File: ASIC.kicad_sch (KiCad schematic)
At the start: 74 parts, among them U12 TLV75512PDQNR, U14 TLV75512PDQNR, U15 TLV75512PDQNR, U3 TLV75512PDQNR, U8 SN74AVC4T774, Y2 50MHz

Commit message: power plane cleanup. added field vias. generated BOM
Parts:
- Y2: LCSC C5137267 -> (none)
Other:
- moved on the sheet: C19, C25, C26, C27, C28, C57, C58, C59, C68, C7, C72, R26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

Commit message: update TPS546D24 to `S` variant. Add render and readme.
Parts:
- TP18, TP2, TP3, TP4, TP58, TP59, TP60: now left out of the parts list
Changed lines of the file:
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@@
 		(unit 1)
 		(exclude_from_sim yes)
-		(in_bom yes)
+		(in_bom no)
 		(on_board yes)
 		(dnp no)
@@
 		(unit 1)
 		(exclude_from_sim yes)
-		(in_bom yes)
+		(in_bom no)
 		(on_board yes)
 		(dnp no)
@@
 		(unit 1)
 		(exclude_from_sim yes)
-		(in_bom yes)
+		(in_bom no)
 		(on_board yes)
 		(dnp no)
@@
 		(unit 1)
 		(exclude_from_sim yes)
-		(in_bom yes)
+		(in_bom no)
 		(on_board yes)
 		(dnp no)
@@
 		(unit 1)
 		(exclude_from_sim yes)
-		(in_bom yes)
+		(in_bom no)
 		(on_board yes)
 		(dnp no)
@@
 		(unit 1)
 		(exclude_from_sim yes)
-		(in_bom yes)
+		(in_bom no)
 		(on_board yes)
 		(dnp no)
@@
 		(unit 1)
 		(exclude_from_sim yes)
-		(in_bom yes)
+		(in_bom no)
 		(on_board yes)
 		(dnp no)

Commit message: unify 1k resistor part numbers
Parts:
- U8: value SN74AVC4T774 -> SN74AXC4T774
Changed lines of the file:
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@@
 			)
 		)
-		(property "Value" "SN74AVC4T774"
+		(property "Value" "SN74AXC4T774"
 			(at 502.92 306.07 0)
 			(effects

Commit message: update 50MHz osc part number.
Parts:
- Y2: DK (none) -> ECS-3225MV-500-CN-TR; PARTNO SX3M50.000E20F30THN -> XC2889CT-ND
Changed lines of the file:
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@@
 			)
 		)
-		(property "DK" ""
+		(property "DK" "ECS-3225MV-500-CN-TR"
 			(at 62.23 320.04 0)
 			(effects
@@
 			)
 		)
-		(property "PARTNO" "SX3M50.000E20F30THN"
+		(property "PARTNO" "XC2889CT-ND"
 			(at 62.23 320.04 0)
 			(effects

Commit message: change Y2 OSC part number back.
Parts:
- Y2: DK ECS-3225MV-500-CN-TR -> 5852-SX3M50.000E20F30THNTR-ND; LCSC (none) -> C5137267; PARTNO XC2889CT-ND -> SX3M50.000E20F30THN
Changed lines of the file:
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@@
 			)
 		)
-		(property "DK" "ECS-3225MV-500-CN-TR"
+		(property "DK" "5852-SX3M50.000E20F30THNTR-ND"
 			(at 62.23 320.04 0)
 			(effects
@@
 			)
 		)
-		(property "PARTNO" "XC2889CT-ND"
+		(property "PARTNO" "SX3M50.000E20F30THN"
 			(at 62.23 320.04 0)
 			(effects
@@
 			)
 		)
-		(property "LCSC" ""
+		(property "LCSC" "C5137267"
 			(at 62.23 320.04 0)
 			(effects

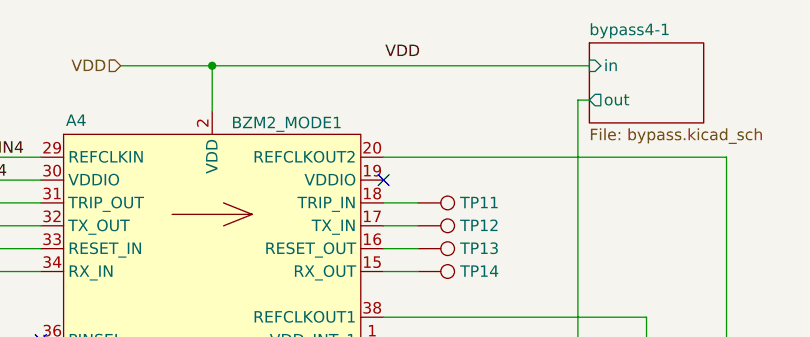
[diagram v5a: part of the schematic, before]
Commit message: clean up some of the schematic errors for #4
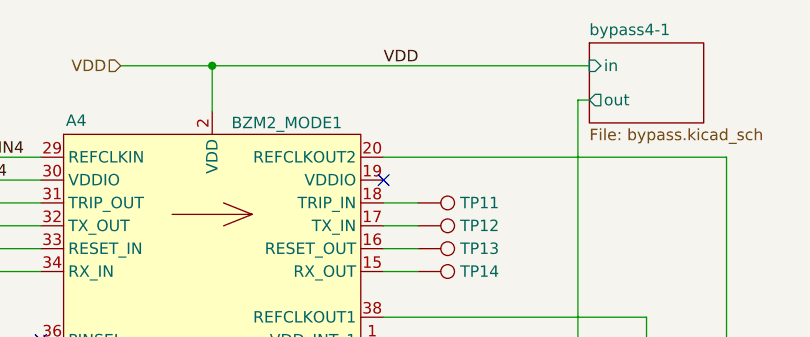
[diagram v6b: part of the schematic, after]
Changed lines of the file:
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@@
 	)
 	(label "VDD"
-		(at 306.2448 61.6474 0)
+		(at 306.07 62.23 0)
 		(effects
 			(font

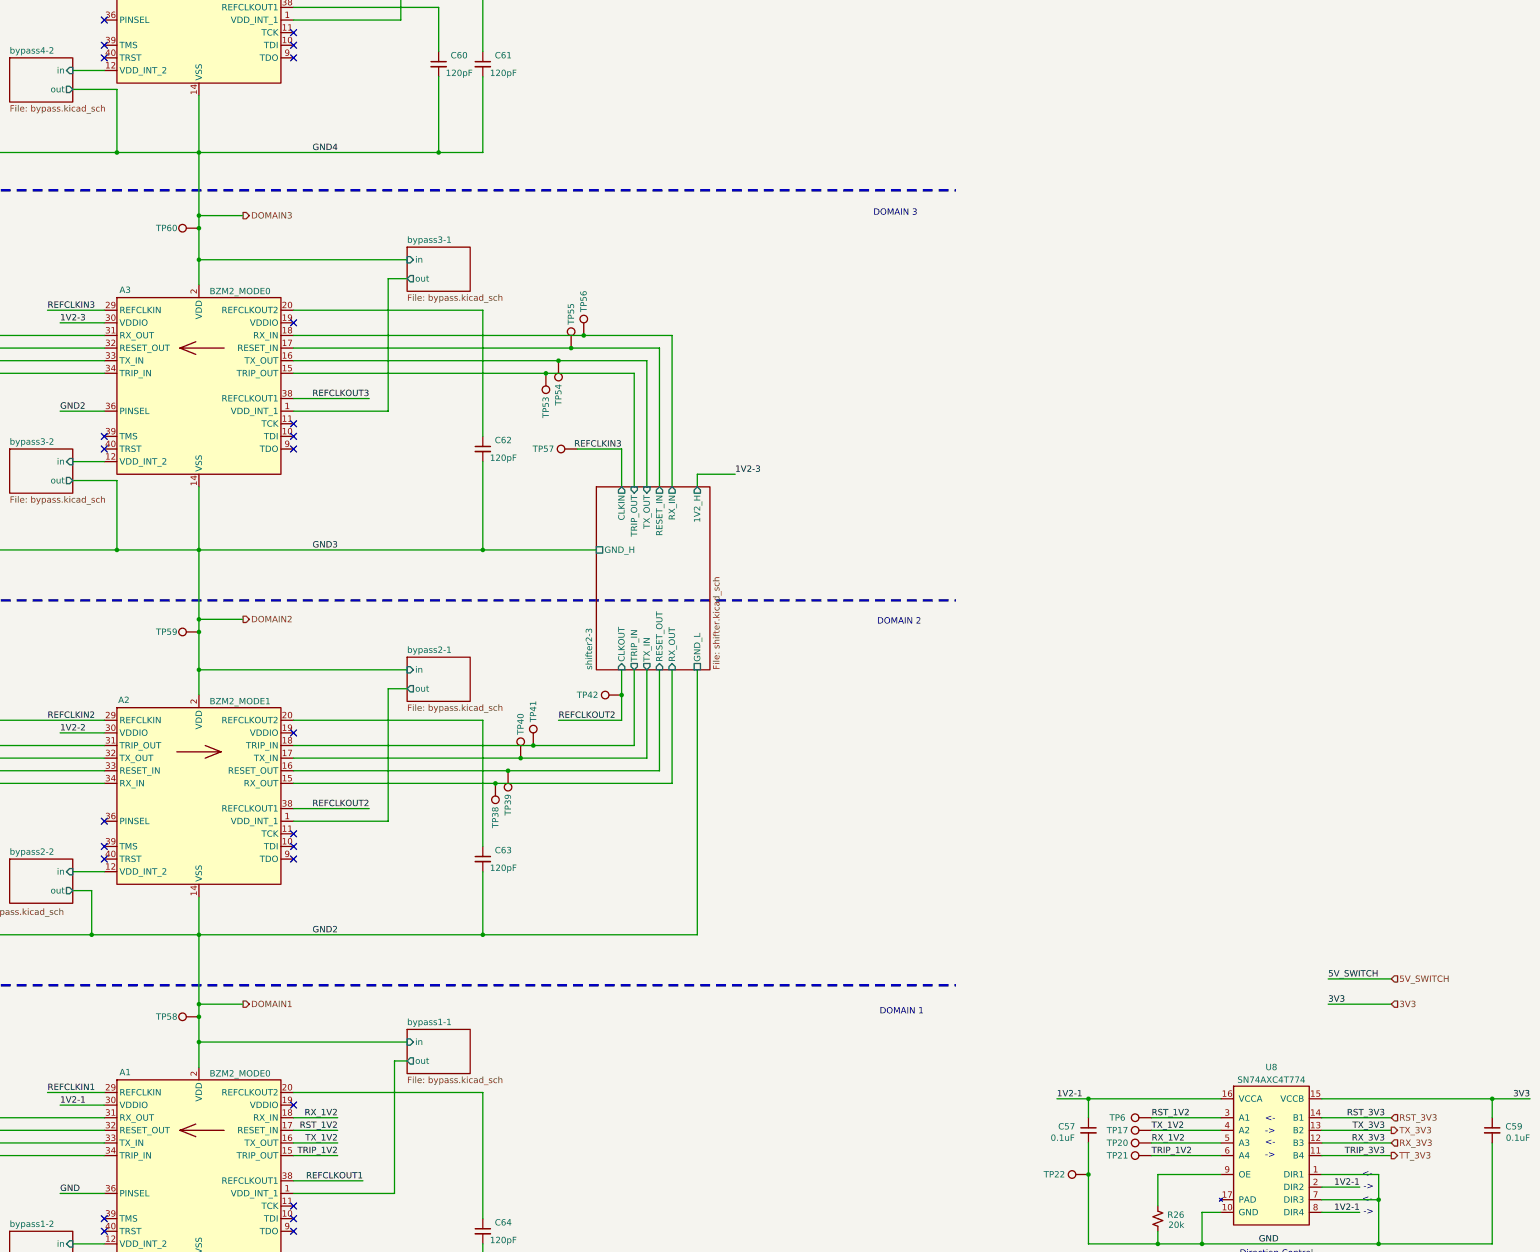
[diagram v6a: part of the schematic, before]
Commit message: cleaned up lots of ERC errors and warnings for #4
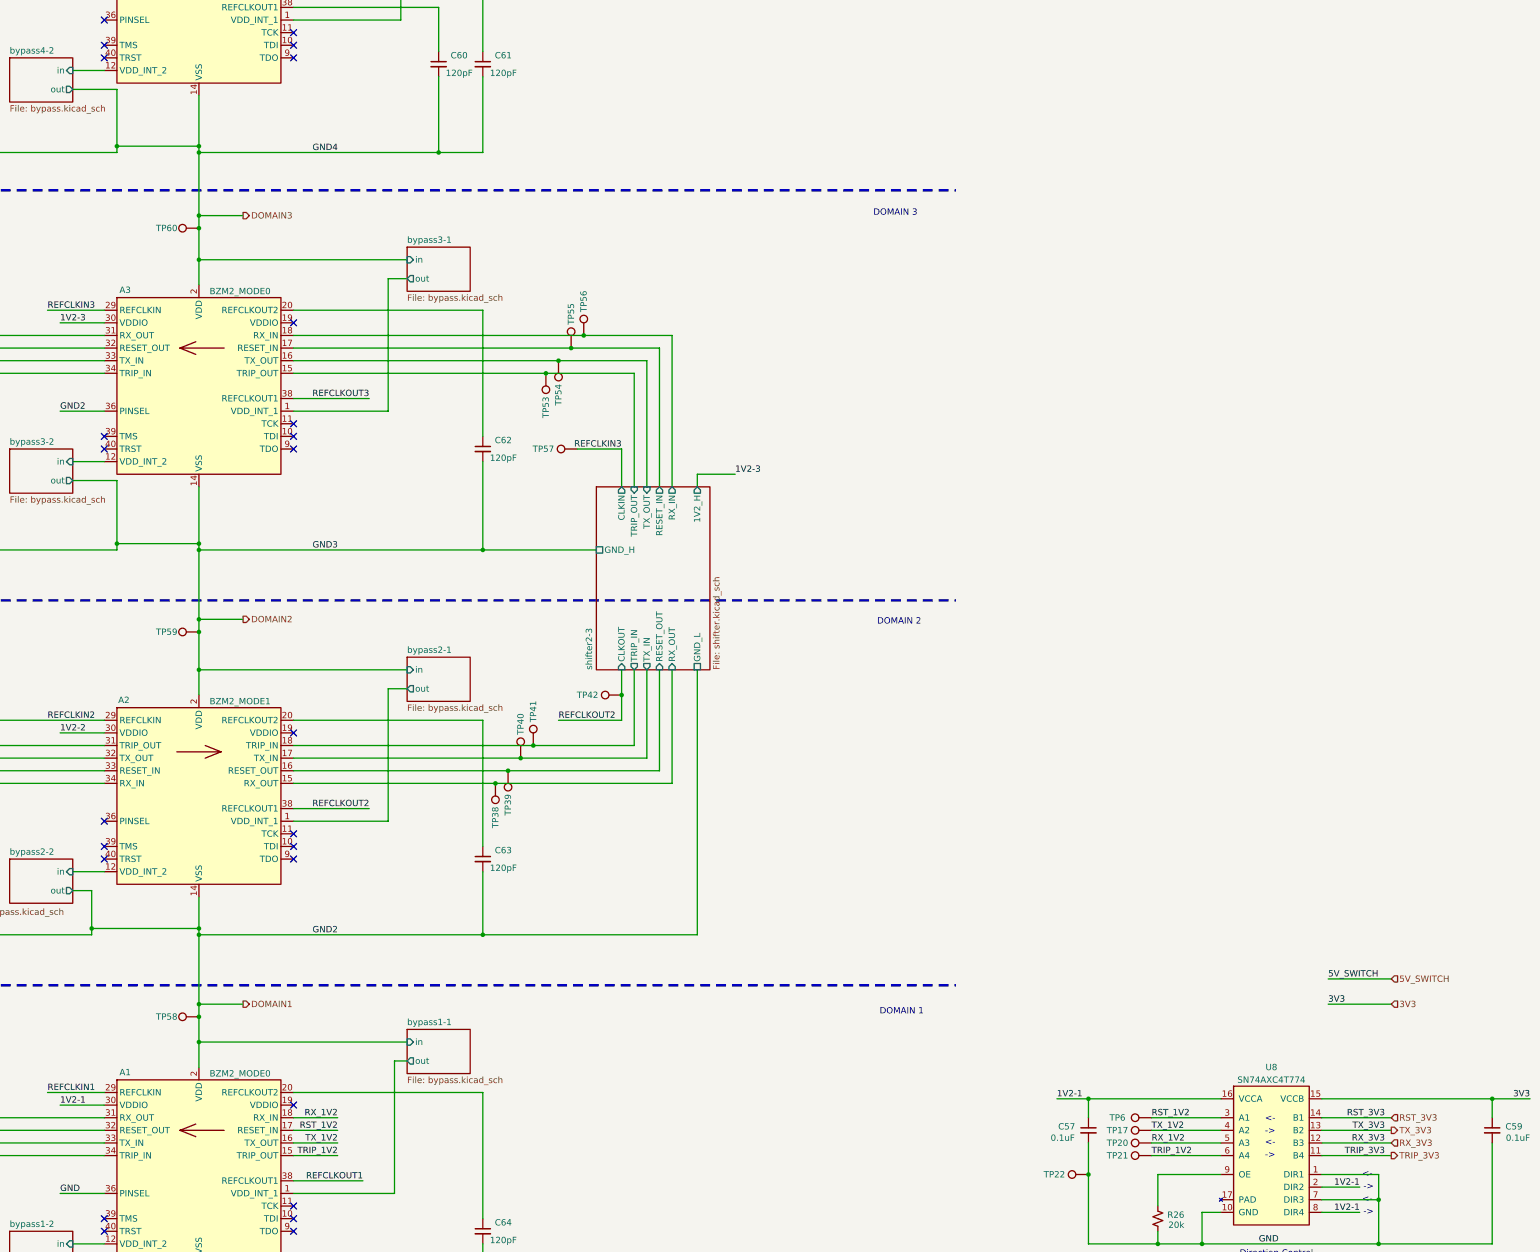
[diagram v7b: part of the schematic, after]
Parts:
- U8: Partnum (none) -> SN74AXC4T774BQBR
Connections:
- net TT_3V3 renamed TRIP_3V3

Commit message: fix part numbers for C60-C64 for #5
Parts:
- C60, C61, C62, C63, C64: DK 1292-1639-1-ND -> 490-16458-1-ND; PARTNO 0402X104K100CT -> GCM1555C1H121FA16D
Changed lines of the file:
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@@
 			)
 		)
-		(property "DK" "1292-1639-1-ND"
+		(property "DK" "490-16458-1-ND"
 			(at 335.28 101.6 0)
 			(effects
@@
 			)
 		)
-		(property "PARTNO" "0402X104K100CT"
+		(property "PARTNO" "GCM1555C1H121FA16D"
 			(at 335.28 101.6 0)
 			(effects
@@
 			)
 		)
-		(property "DK" "1292-1639-1-ND"
+		(property "DK" "490-16458-1-ND"
 			(at 344.17 179.07 0)
 			(effects
@@
 			)
 		)
-		(property "PARTNO" "0402X104K100CT"
+		(property "PARTNO" "GCM1555C1H121FA16D"
 			(at 344.17 179.07 0)
 			(effects
@@
 			)
 		)
-		(property "DK" "1292-1639-1-ND"
+		(property "DK" "490-16458-1-ND"
 			(at 344.17 336.55 0)
 			(effects
@@
 			)
 		)
-		(property "PARTNO" "0402X104K100CT"
+		(property "PARTNO" "GCM1555C1H121FA16D"
 			(at 344.17 336.55 0)
 			(effects
@@
 			)
 		)
-		(property "DK" "1292-1639-1-ND"
+		(property "DK" "490-16458-1-ND"
 			(at 344.17 261.62 0)
 			(effects
@@
 			)
 		)
-		(property "PARTNO" "0402X104K100CT"
+		(property "PARTNO" "GCM1555C1H121FA16D"
 			(at 344.17 261.62 0)
 			(effects
@@
 			)
 		)
-		(property "DK" "1292-1639-1-ND"
+		(property "DK" "490-16458-1-ND"
 			(at 344.17 101.6 0)
 			(effects
@@
 			)
 		)
-		(property "PARTNO" "0402X104K100CT"
+		(property "PARTNO" "GCM1555C1H121FA16D"
 			(at 344.17 101.6 0)
 			(effects
